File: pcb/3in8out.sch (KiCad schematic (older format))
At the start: 15 parts, among them Q6 CSC388A, Q7 CSC388A, Q8 CSC388A, U4 74HC00, U5 74HC00, U6 74HC00

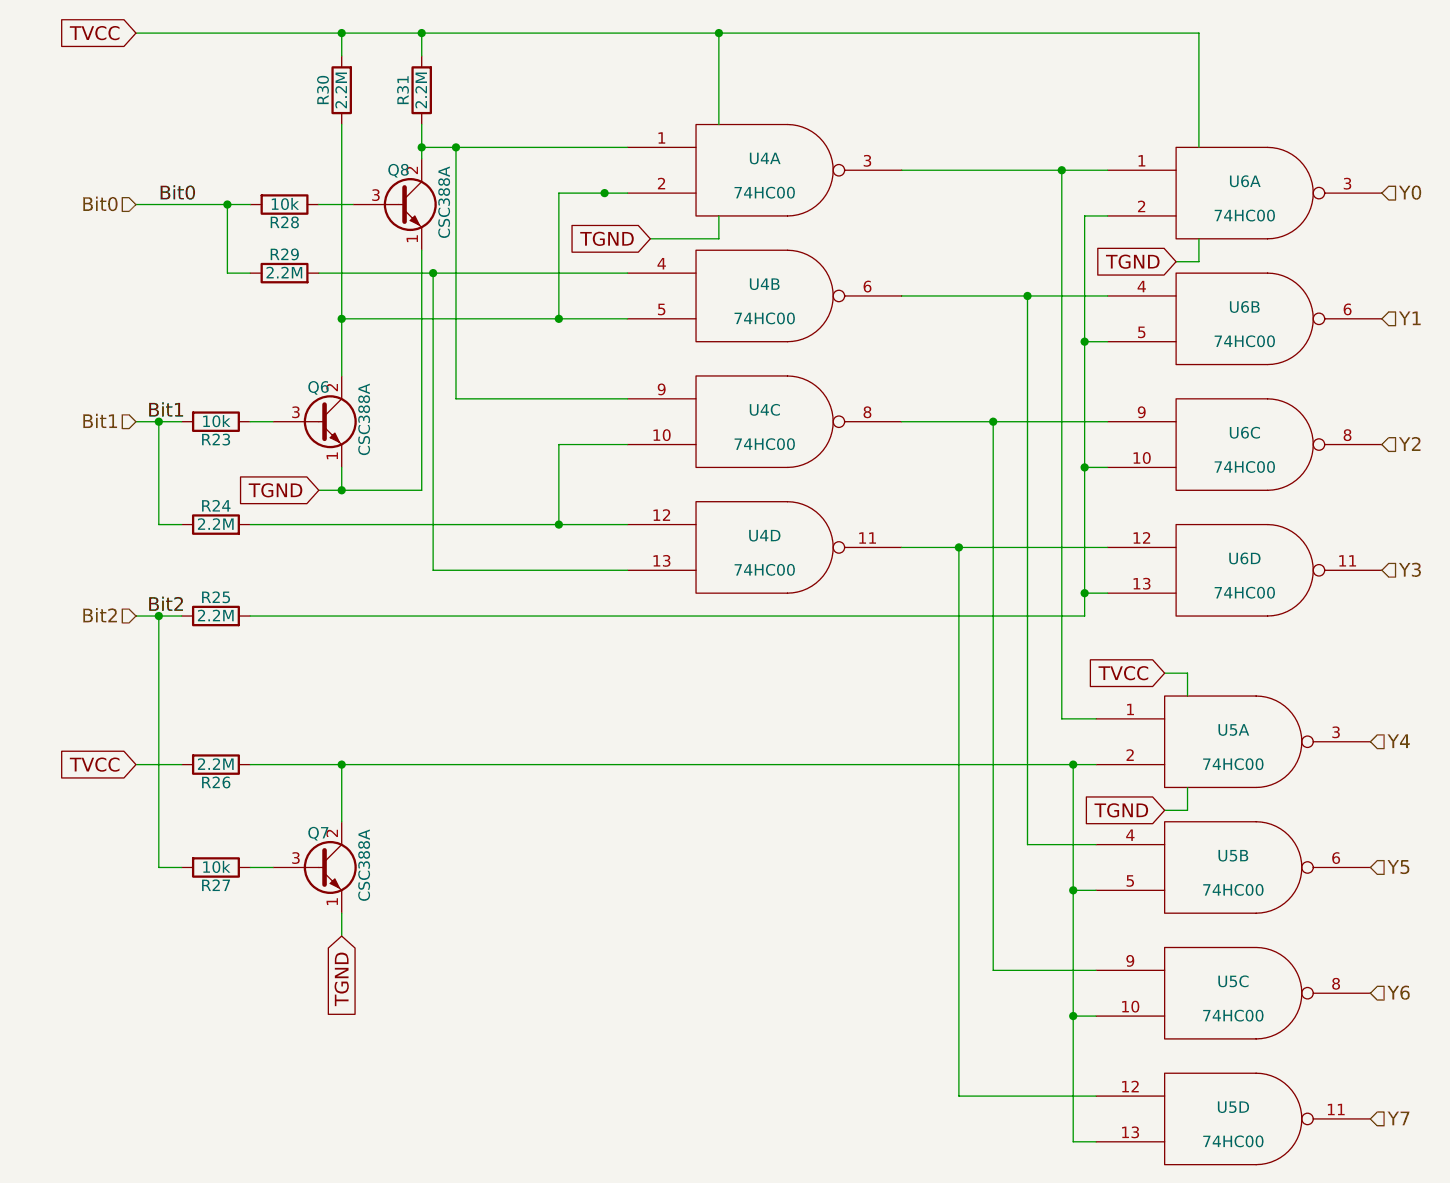
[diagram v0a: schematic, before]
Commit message: 基本的に入出力に関する，7SEG, LED, PUSH-BUTTONを2階に配置する。
2階-1階の直登戦術でいこうと思う。
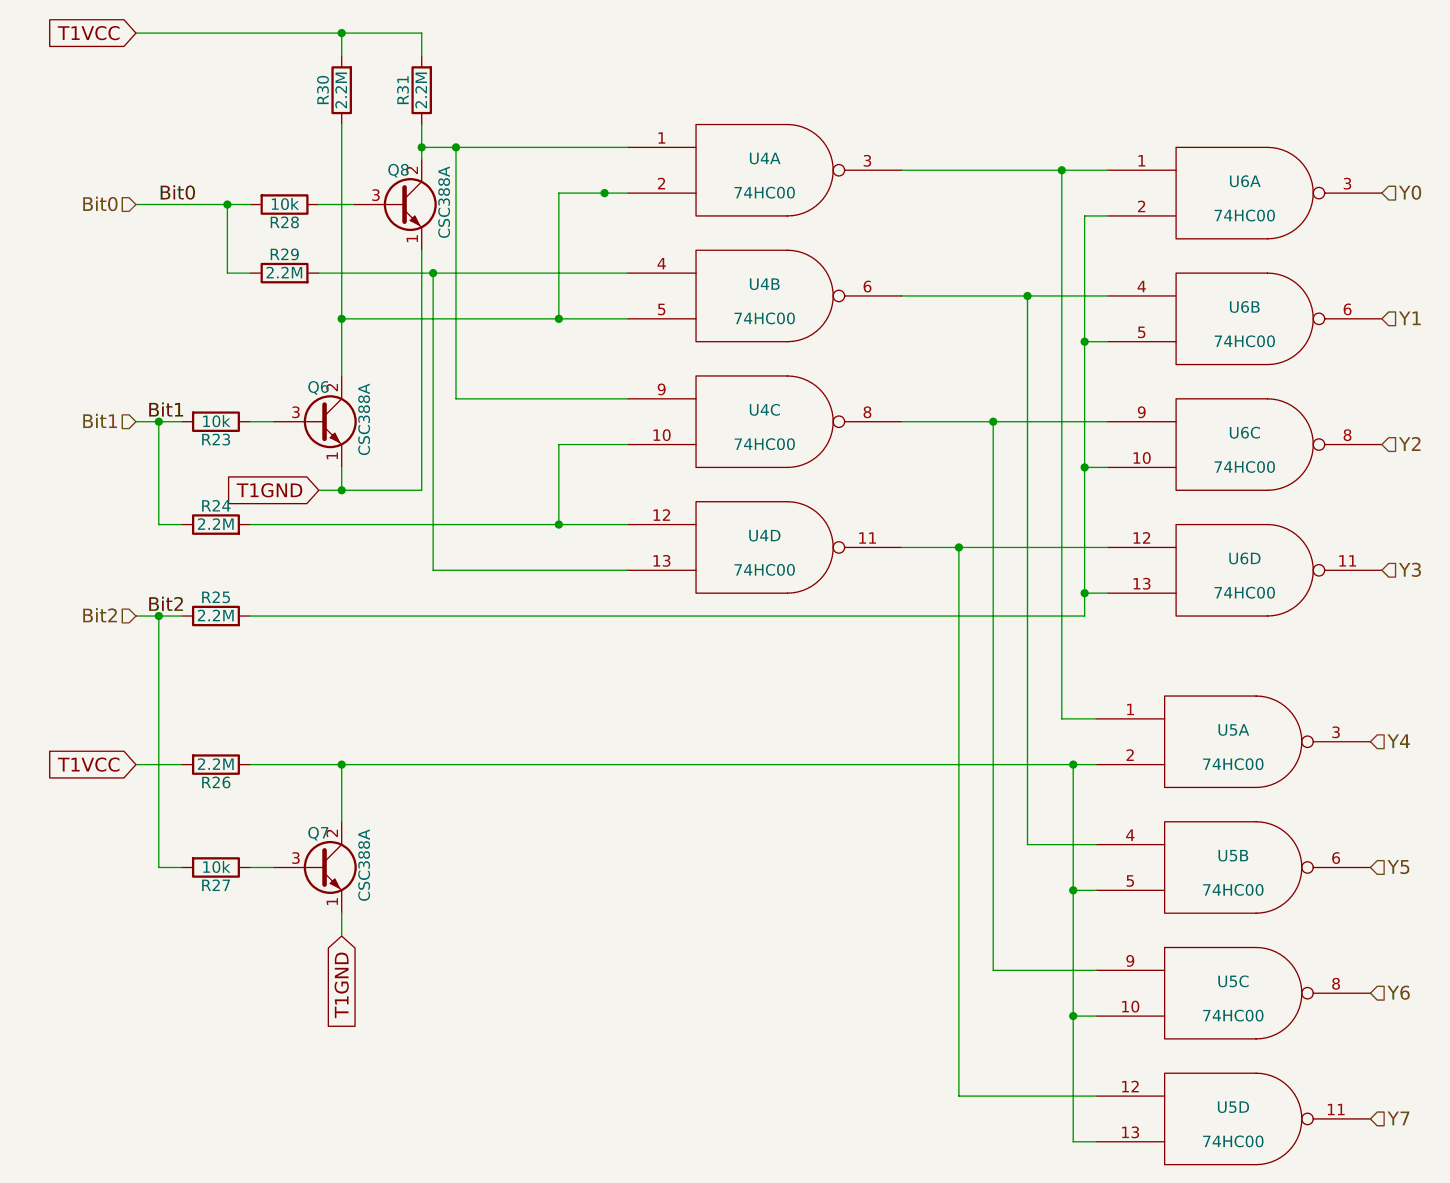
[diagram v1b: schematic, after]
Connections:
- net GND_T1: no longer Q6.1 (E), Q7.1 (E), Q8.1 (E)
- net VCC_T1: no longer R26.2, R30.2, R31.2
- new net T1GND: Q6.1 (E), Q7.1 (E), Q8.1 (E)
- new net T1VCC: R26.2, R30.2, R31.2
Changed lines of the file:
@@
 Y7
 Text GLabel 2600 4250 0    60   Input ~ 0
-TVCC
-Text GLabel 3500 5000 3    60   Input ~ 0
-TGND
+T1VCC
 Text GLabel 2600 1050 0    60   Input ~ 0
-TVCC
+T1VCC
 Text GLabel 3400 3050 0    60   Input ~ 0
-TGND
+T1GND
 Wire Wire Line
 	3400 1800 3550 1800
@@
 Connection ~ 6750 3500
 Wire Wire Line
-	2600 1050 7250 1050
-Wire Wire Line
 	3850 1050 3850 1150
 Wire Wire Line
@@
 Wire Wire Line
 	6800 5700 6200 5700
-Wire Wire Line
-	5150 1050 5150 1450
-Connection ~ 3850 1050
-Connection ~ 5150 1050
-Text GLabel 7100 3850 0    60   Input ~ 0
-TVCC
-Wire Wire Line
-	7100 3850 7200 3850
-Wire Wire Line
-	7200 3850 7200 3950
-Wire Wire Line
-	5150 1950 5150 1850
-Wire Wire Line
-	4850 1950 5150 1950
 Connection ~ 4650 1750
-Wire Wire Line
-	7250 1950 7250 2050
-Wire Wire Line
-	7200 4350 7200 4450
-Text GLabel 4850 1950 0    60   Input ~ 0
-TGND
-Text GLabel 7150 2050 0    60   Input ~ 0
-TGND
-Wire Wire Line
-	7250 2050 7150 2050
-Text GLabel 7100 4450 0    60   Input ~ 0
-TGND
-Wire Wire Line
-	7200 4450 7100 4450
-Wire Wire Line
-	7250 1050 7250 1550
 Text Label 2700 1800 0    60   ~ 0
 Bit0
@@
 Text Label 2650 3600 0    60   ~ 0
 Bit2
+Text GLabel 3500 5000 3    60   Input ~ 0
+T1GND
+Wire Wire Line
+	2600 1050 3850 1050
 $EndSCHEMATC

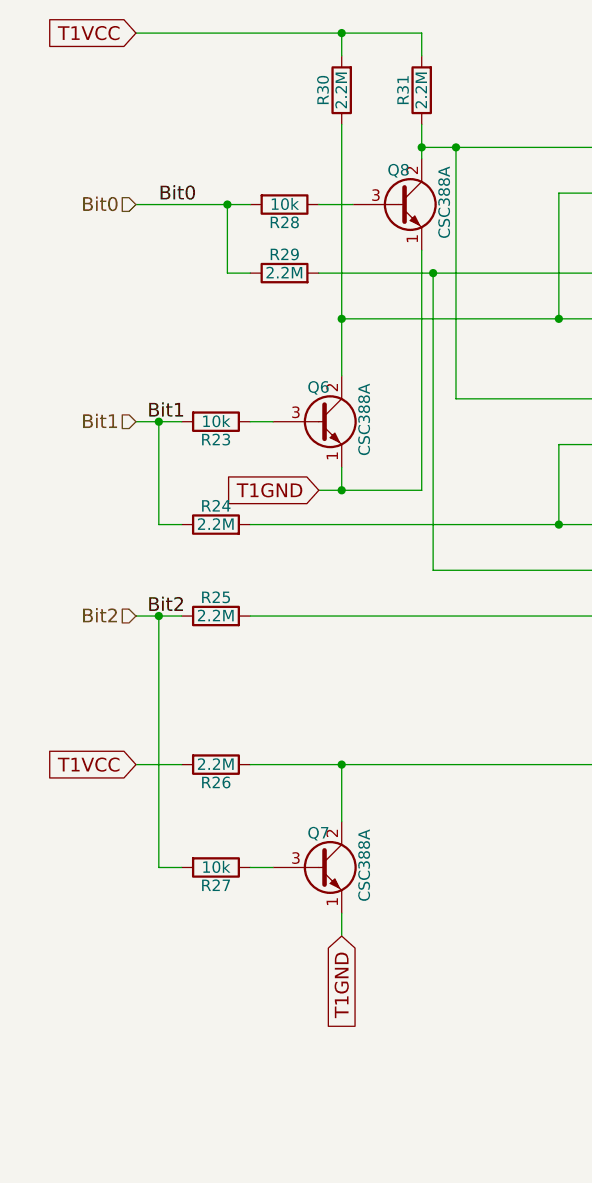
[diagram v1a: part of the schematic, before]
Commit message: 74HC00系用に，VCC_T1, GND_T1を作成。
母板と74HC00をconnectorで分離したかったため，xxx_T1を作成する必要があった。
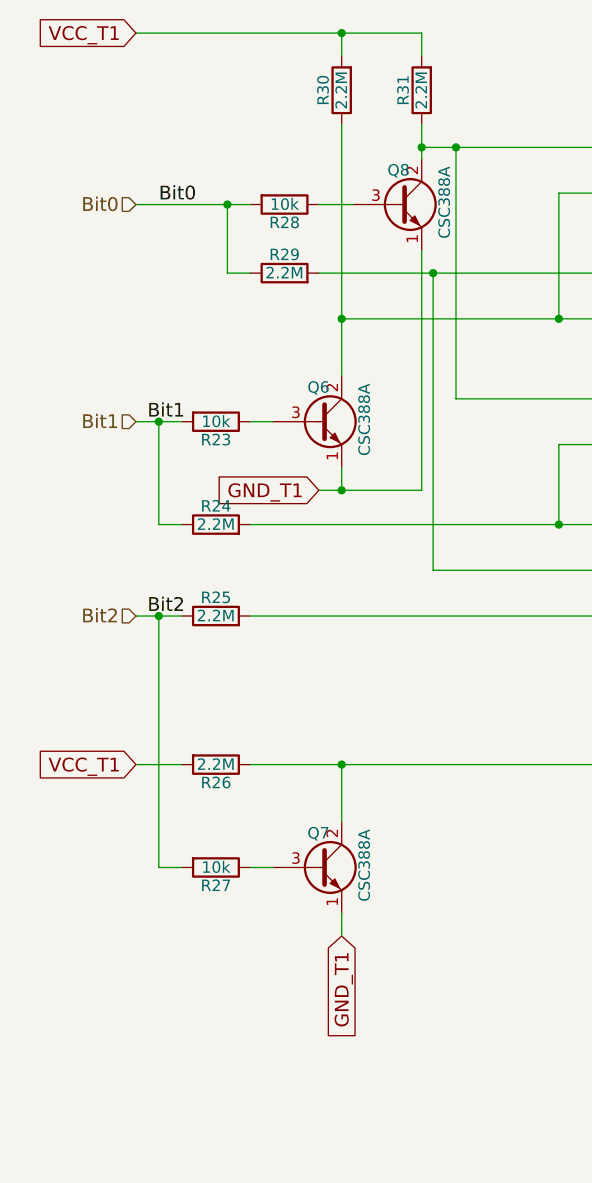
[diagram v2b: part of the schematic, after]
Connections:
- net T1GND is gone; now on net GND_T1: Q6.1 (E), Q7.1 (E), Q8.1 (E)
- net T1VCC is gone; now on net VCC_T1: R26.2, R30.2, R31.2
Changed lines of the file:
@@
 Y7
 Text GLabel 2600 4250 0    60   Input ~ 0
-T1VCC
+VCC_T1
 Text GLabel 2600 1050 0    60   Input ~ 0
-T1VCC
+VCC_T1
 Text GLabel 3400 3050 0    60   Input ~ 0
-T1GND
+GND_T1
 Wire Wire Line
 	3400 1800 3550 1800
@@
 Bit2
 Text GLabel 3500 5000 3    60   Input ~ 0
-T1GND
+GND_T1
 Wire Wire Line
 	2600 1050 3850 1050

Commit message: transistor には，CvPcbをやり直した。
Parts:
- Q6, Q7, Q8: footprint TO_SOT_Packages_THT:TO-92_Inline_Wide -> Package_TO_SOT_THT:TO-92_Inline_Wide
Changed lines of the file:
@@
 F 0 "Q8" H 3700 1950 50  0000 L CNN
 F 1 "CSC388A" V 3950 1650 50  0000 L CNN
-F 2 "TO_SOT_Packages_THT:TO-92_Inline_Wide" H 3950 1725 50  0001 L CIN
+F 2 "Package_TO_SOT_THT:TO-92_Inline_Wide" H 3950 1725 50  0001 L CIN
 F 3 "" H 3750 1800 50  0001 L CNN
 	1    3750 1800
@@
 F 0 "Q6" H 3350 2900 50  0000 L CNN
 F 1 "CSC388A" V 3600 2600 50  0000 L CNN
-F 2 "TO_SOT_Packages_THT:TO-92_Inline_Wide" H 3600 2675 50  0001 L CIN
+F 2 "Package_TO_SOT_THT:TO-92_Inline_Wide" H 3600 2675 50  0001 L CIN
 F 3 "" H 3400 2750 50  0001 L CNN
 	1    3400 2750
@@
 F 0 "Q7" H 3350 4850 50  0000 L CNN
 F 1 "CSC388A" V 3600 4550 50  0000 L CNN
-F 2 "TO_SOT_Packages_THT:TO-92_Inline_Wide" H 3600 4625 50  0001 L CIN
+F 2 "Package_TO_SOT_THT:TO-92_Inline_Wide" H 3600 4625 50  0001 L CIN
 F 3 "" H 3400 4700 50  0001 L CNN
 	1    3400 4700
